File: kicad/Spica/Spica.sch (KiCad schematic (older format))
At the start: 8 parts

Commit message: Add some Akizuki parts
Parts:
- removed R?: R_Variable, symbol Device:R_Variable
- added RV1: 10k, symbol Device:R_POT
- added SW1: SW_SPDT, symbol Switch:SW_SPDT
- IC1: renamed from IC?; symbol SamacSys_Parts:TA48033S -> Spica-rescue:TA48033S-SamacSys_Parts
- U1: renamed from U?; symbol ESP32-DEVKITC-32D:ESP32-DEVKITC-32D -> Spica-rescue:ESP32-DEVKITC-32D-ESP32-DEVKITC-32D
- gave numbers to parts that had none: 5
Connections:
- wire segments 9 -> 18
- no-connect marks 0 -> 28
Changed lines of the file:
@@
 EESchema Schematic File Version 4
+LIBS:Spica-cache
 EELAYER 26 0
 EELAYER END
@@
 $EndDescr
 $Comp
-L ESP32-DEVKITC-32D:ESP32-DEVKITC-32D U?
+L Spica-rescue:ESP32-DEVKITC-32D-ESP32-DEVKITC-32D U1
 U 1 1 5BDC6C5C
 P 8600 3300
-F 0 "U?" H 8600 4467 50  0000 C CNN
+F 0 "U1" H 8600 4467 50  0000 C CNN
 F 1 "ESP32-DEVKITC-32D" H 8600 4376 50  0000 C CNN
 F 2 "MODULE_ESP32-DEVKITC-32D" H 8600 3300 50  0001 L BNN
@@
 $EndComp
 $Comp
-L Motor:Motor_DC M?
+L Motor:Motor_DC M2
 U 1 1 5BDC7764
 P 3000 1650
-F 0 "M?" H 3158 1646 50  0000 L CNN
+F 0 "M2" H 3158 1646 50  0000 L CNN
 F 1 "Motor_DC" H 3158 1555 50  0000 L CNN
 F 2 "Connector_JST:JST_XH_B02B-XH-A_1x02_P2.50mm_Vertical" H 3000 1560 50  0001 C CNN
@@
 $EndComp
 $Comp
-L Motor:Motor_DC M?
+L Motor:Motor_DC M1
 U 1 1 5BDC782D
 P 2250 1650
-F 0 "M?" H 2408 1646 50  0000 L CNN
+F 0 "M1" H 2408 1646 50  0000 L CNN
 F 1 "Motor_DC" H 2408 1555 50  0000 L CNN
 F 2 "Connector_JST:JST_XH_B02B-XH-A_1x02_P2.50mm_Vertical" H 2250 1560 50  0001 C CNN
@@
 $EndComp
 $Comp
-L SamacSys_Parts:TA48033S IC?
+L Spica-rescue:TA48033S-SamacSys_Parts IC1
 U 1 1 5BDC796A
 P 2700 4100
-F 0 "IC?" H 3200 4365 50  0000 C CNN
+F 0 "IC1" H 3200 4365 50  0000 C CNN
 F 1 "TA48033S" H 3200 4274 50  0000 C CNN
 F 2 "TO254P490X1000X2090-3P" H 3550 4200 50  0001 L CNN
@@
 L power:VCC #PWR0101
 U 1 1 5BDC7FCD
-P 1150 4100
-F 0 "#PWR0101" H 1150 3950 50  0001 C CNN
-F 1 "VCC" H 1167 4273 50  0000 C CNN
-F 2 "" H 1150 4100 50  0001 C CNN
-F 3 "" H 1150 4100 50  0001 C CNN
-	1    1150 4100
+P 750 4100
+F 0 "#PWR0101" H 750 3950 50  0001 C CNN
+F 1 "VCC" H 767 4273 50  0000 C CNN
+F 2 "" H 750 4100 50  0001 C CNN
+F 3 "" H 750 4100 50  0001 C CNN
+	1    750  4100
 	1    0    0    -1
 $EndComp
@@
 $EndComp
 $Comp
-L Device:C C?
+L Device:C C2
 U 1 1 5BDC8EDA
 P 2200 4250
-F 0 "C?" H 2315 4296 50  0000 L CNN
+F 0 "C2" H 2315 4296 50  0000 L CNN
 F 1 "C" H 2315 4205 50  0000 L CNN
 F 2 "" H 2238 4100 50  0001 C CNN
@@
 $EndComp
 $Comp
-L Device:CP C?
+L Device:CP C3
 U 1 1 5BDC96DE
 P 3900 4250
-F 0 "C?" H 4018 4296 50  0000 L CNN
+F 0 "C3" H 4018 4296 50  0000 L CNN
 F 1 "CP" H 4018 4205 50  0000 L CNN
 F 2 "" H 3938 4100 50  0001 C CNN
@@
 $EndComp
 $Comp
-L Device:CP C?
+L Device:CP C1
 U 1 1 5BDCB405
 P 1850 4250
-F 0 "C?" H 1968 4296 50  0000 L CNN
+F 0 "C1" H 1968 4296 50  0000 L CNN
 F 1 "CP" H 1968 4205 50  0000 L CNN
 F 2 "" H 1888 4100 50  0001 C CNN
@@
 $EndComp
 Wire Wire Line
-	1150 4100 1850 4100
-Wire Wire Line
 	2200 4100 1850 4100
 Connection ~ 2200 4100
+$Comp
+L power:GND #PWR0115
+U 1 1 5BDD17C0
+P 6450 3250
+F 0 "#PWR0115" H 6450 3000 50  0001 C CNN
+F 1 "GND" H 6455 3077 50  0000 C CNN
+F 2 "" H 6450 3250 50  0001 C CNN
+F 3 "" H 6450 3250 50  0001 C CNN
+	1    6450 3250
+	1    0    0    -1
+$EndComp
+$Comp
+L power:+3.3V #PWR0116
+U 1 1 5BDD1968
+P 6450 2950
+F 0 "#PWR0116" H 6450 2800 50  0001 C CNN
+F 1 "+3.3V" H 6465 3123 50  0000 C CNN
+F 2 "" H 6450 2950 50  0001 C CNN
+F 3 "" H 6450 2950 50  0001 C CNN
+	1    6450 2950
+	1    0    0    -1
+$EndComp
+$Comp
+L Switch:SW_SPDT SW1
+U 1 1 5BDD2829
+P 1150 4100
+F 0 "SW1" H 1150 4385 50  0000 C CNN
+F 1 "SW_SPDT" H 1150 4294 50  0000 C CNN
+F 2 "" H 1150 4100 50  0001 C CNN
+F 3 "" H 1150 4100 50  0001 C CNN
+	1    1150 4100
+	1    0    0    -1
+$EndComp
+Wire Wire Line
+	1350 4000 1850 4000
+Wire Wire Line
+	1850 4000 1850 4100
 Connection ~ 1850 4100
-$Comp
-L Device:R_Variable R?
-U 1 1 5BDCC0C1
-P 6950 3350
-F 0 "R?" H 7078 3396 50  0000 L CNN
-F 1 "R_Variable" H 7078 3305 50  0000 L CNN
-F 2 "" V 6880 3350 50  0001 C CNN
-F 3 "~" H 6950 3350 50  0001 C CNN
-	1    6950 3350
-	1    0    0    -1
-$EndComp
+Wire Wire Line
+	950  4100 750  4100
+NoConn ~ 1350 4200
+NoConn ~ 7800 2500
+NoConn ~ 7800 2600
+NoConn ~ 7800 2700
+$Comp
+L Device:R_POT RV1
+U 1 1 5BDD441D
+P 6450 3100
+F 0 "RV1" H 6380 3146 50  0000 R CNN
+F 1 "10k" H 6380 3055 50  0000 R CNN
+F 2 "" H 6450 3100 50  0001 C CNN
+F 3 "~" H 6450 3100 50  0001 C CNN
+	1    6450 3100
+	1    0    0    -1
+$EndComp
+Wire Wire Line
+	6600 3100 7800 3100
+NoConn ~ 7800 2800
+NoConn ~ 7800 2900
+NoConn ~ 7800 3000
+NoConn ~ 7800 3400
+NoConn ~ 7800 3500
+NoConn ~ 7800 3600
+NoConn ~ 7800 3800
+NoConn ~ 7800 3900
+NoConn ~ 7800 4000
+NoConn ~ 7800 4100
+NoConn ~ 7800 4200
+Wire Wire Line
+	9400 2500 10100 2500
+Wire Wire Line
+	9400 2600 10100 2600
+NoConn ~ 9400 2700
+NoConn ~ 9400 2800
+NoConn ~ 9400 2900
+Wire Wire Line
+	9400 3400 10100 3400
+Wire Wire Line
+	9400 3500 10100 3500
+NoConn ~ 9400 3100
+NoConn ~ 9400 3200
+NoConn ~ 9400 3300
+NoConn ~ 9400 3600
+NoConn ~ 9400 3700
+NoConn ~ 9400 3800
+NoConn ~ 9400 3900
+NoConn ~ 9400 4000
+NoConn ~ 9400 4100
+NoConn ~ 9400 4200
+Wire Wire Line
+	7800 3200 7250 3200
+Wire Wire Line
+	7800 3300 7250 3300
 $EndSCHEMATC

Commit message: Finish rooting
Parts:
- added BT1: Battery_Cell, Connector_JST:JST_XH_B02B-XH-A_1x02_P2.50mm_Vertical, symbol Device:Battery_Cell
- added U2: DRV8835-akizuki, Package_DIP:DIP-12_W7.62mm_LongPads, symbol drv8835-akizuki:DRV8835-akizuki
- added U3: HC-SR04, HC-SR04:XCVR_HC-SR04, symbol HC-SR04:HC-SR04
- added U4: AE-XCL102D503CR-G, Package_DIP:DIP-6_W7.62mm_Socket, symbol xcl102-akizuki:AE-XCL102D503CR-G
- C1: value CP -> 1000μ; footprint (none) -> Capacitor_THT:CP_Radial_D10.0mm_P5.00mm
- C2: value C -> 0.1μ; footprint (none) -> Capacitor_THT:C_Disc_D3.0mm_W2.0mm_P2.50mm
- C3: value CP -> 100μ; footprint (none) -> Capacitor_THT:CP_Radial_D5.0mm_P2.50mm
- IC1: symbol Spica-rescue:TA48033S-SamacSys_Parts -> TA48033S:TA48033S
- RV1: footprint (none) -> TSR-065-103-R:TSR065103R
- SW1: footprint (none) -> Connector_PinSocket_2.54mm:PinSocket_1x03_P2.54mm_Vertical
- U1: symbol Spica-rescue:ESP32-DEVKITC-32D-ESP32-DEVKITC-32D -> ESP32-DEVKITC-32D:ESP32-DEVKITC-32D
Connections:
- net labels added: 3.3V, 5V, IO16, IO17, IO22, IO23, IO25, IO26
- net labels removed: +3.3V
- wire segments 18 -> 33
- no-connect marks 28 -> 29
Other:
- moved on the sheet: C1, C2, C3, IC1, M1, M2, SW1

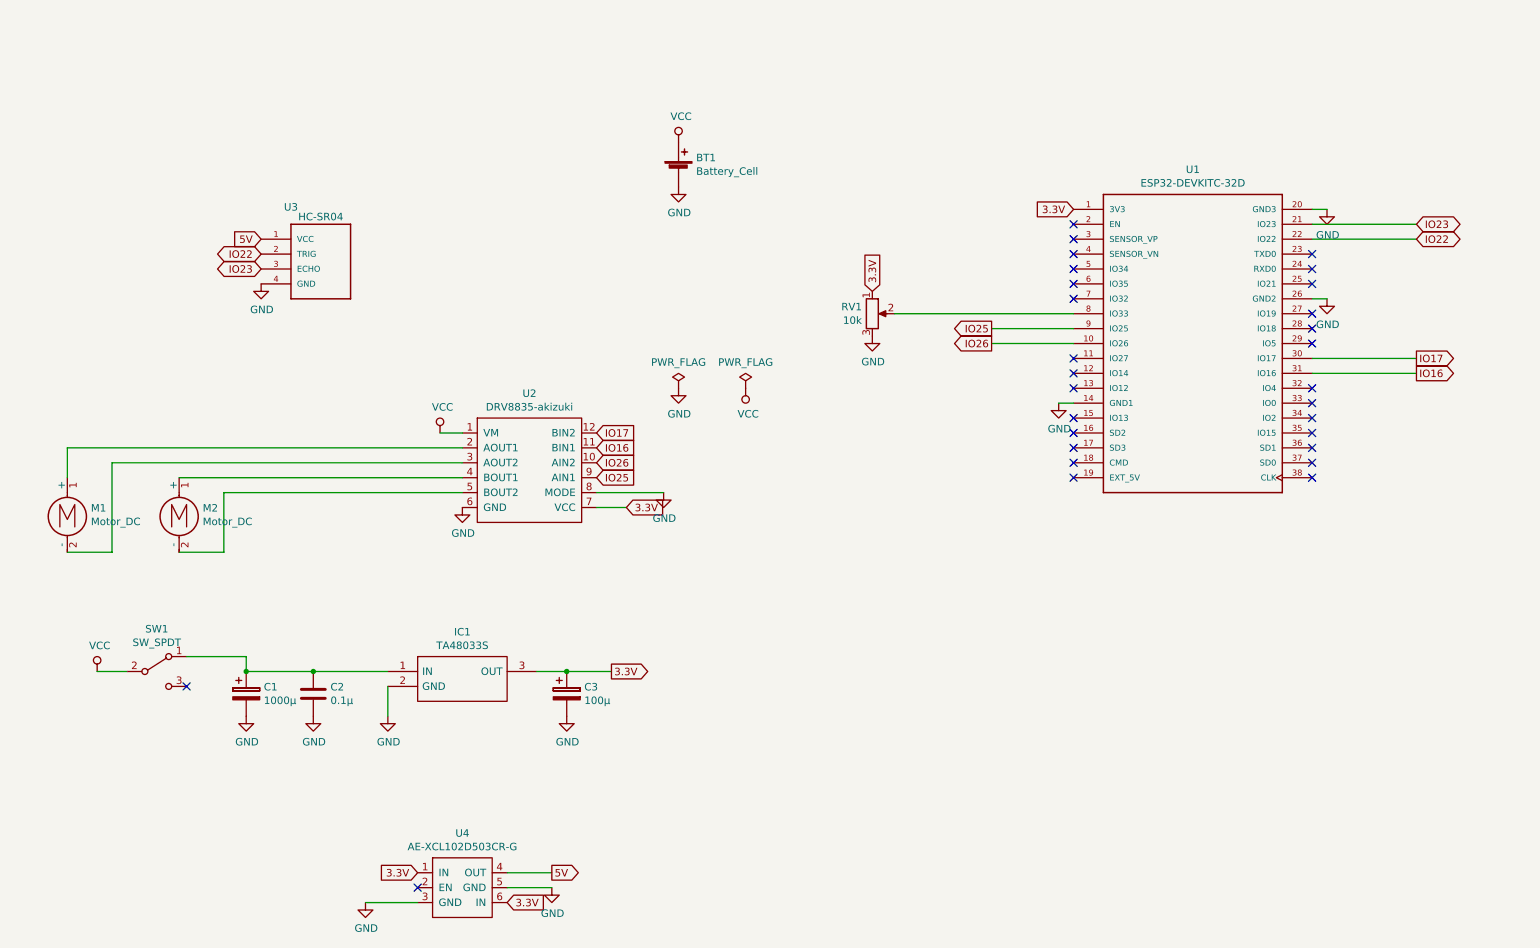
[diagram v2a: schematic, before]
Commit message: Add surface GND
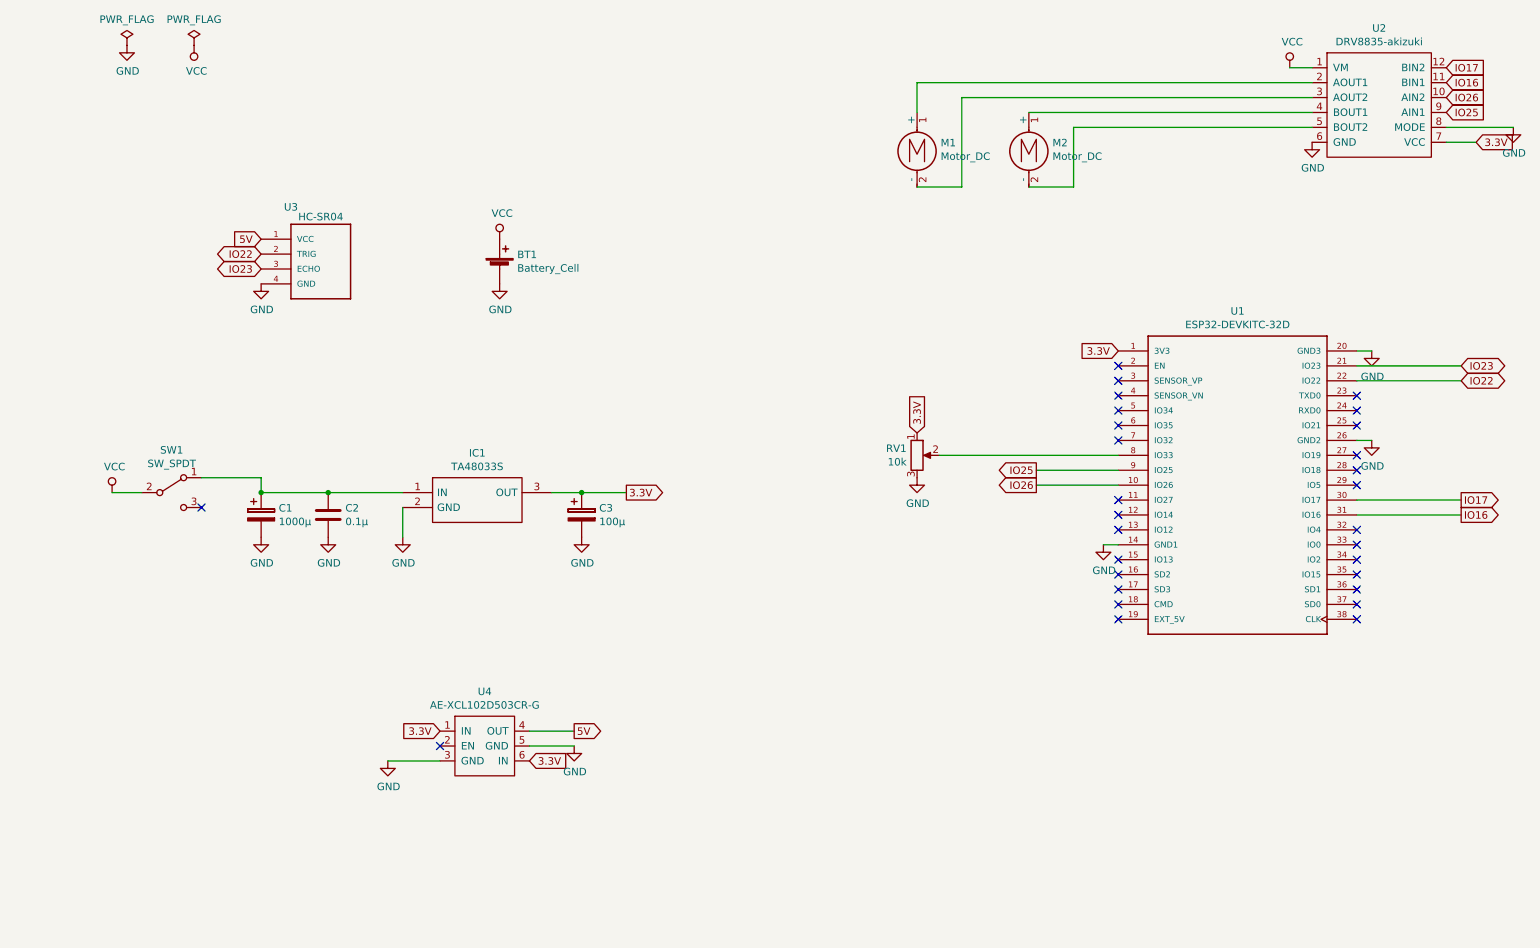
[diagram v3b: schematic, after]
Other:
- moved on the sheet: BT1, C1, C2, C3, IC1, M1, M2, RV1, SW1, U1, U2, U4

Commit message: ベタパターンを追加
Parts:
- added C4: 0.1μ, Capacitor_THT:C_Disc_D3.0mm_W2.0mm_P2.50mm, symbol Device:C
- added C5: 10μ, Capacitor_THT:CP_Radial_D5.0mm_P2.50mm, symbol Device:CP
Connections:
- net 3.3V: now also C4.1
- net 5V: now also C5.1
- net GND: now also C4.2, C5.2
- net VCC: now also C1.1, C2.1, IC1.1 (IN); no longer BT1.1 (+)
- new net: BT1.1 (+), SW1.1 (A)
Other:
- moved on the sheet: SW1
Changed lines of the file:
@@
 L power:VCC #PWR0101
 U 1 1 5BDC7FCD
-P 1350 4300
-F 0 "#PWR0101" H 1350 4150 50  0001 C CNN
-F 1 "VCC" H 1367 4473 50  0000 C CNN
-F 2 "" H 1350 4300 50  0001 C CNN
-F 3 "" H 1350 4300 50  0001 C CNN
-	1    1350 4300
+P 2350 4200
+F 0 "#PWR0101" H 2350 4050 50  0001 C CNN
+F 1 "VCC" H 2367 4373 50  0000 C CNN
+F 2 "" H 2350 4200 50  0001 C CNN
+F 3 "" H 2350 4200 50  0001 C CNN
+	1    2350 4200
 	1    0    0    -1
 $EndComp
@@
 	4300 4300 4500 4300
 Wire Wire Line
-	4800 4300 4500 4300
-Connection ~ 4500 4300
-Wire Wire Line
 	3300 4400 3300 4600
 Wire Wire Line
@@
 L Switch:SW_SPDT SW1
 U 1 1 5BDD2829
-P 1750 4300
-F 0 "SW1" H 1750 4585 50  0000 C CNN
-F 1 "SW_SPDT" H 1750 4494 50  0000 C CNN
-F 2 "Connector_PinSocket_2.54mm:PinSocket_1x03_P2.54mm_Vertical" H 1750 4300 50  0001 C CNN
-F 3 "" H 1750 4300 50  0001 C CNN
-	1    1750 4300
-	1    0    0    -1
-$EndComp
-Wire Wire Line
-	1950 4200 2350 4200
+P 3850 2000
+F 0 "SW1" H 3850 2285 50  0000 C CNN
+F 1 "SW_SPDT" H 3850 2194 50  0000 C CNN
+F 2 "Connector_PinSocket_2.54mm:PinSocket_1x03_P2.54mm_Vertical" H 3850 2000 50  0001 C CNN
+F 3 "" H 3850 2000 50  0001 C CNN
+	1    3850 2000
+	0    1    1    0
+$EndComp
+Wire Wire Line
+	3950 2200 3950 2600
 Wire Wire Line
 	2350 4200 2350 4300
 Wire Wire Line
-	1550 4300 1350 4300
-NoConn ~ 1950 4400
+	3850 1800 3850 1600
+NoConn ~ 3750 2200
 NoConn ~ 8100 3450
 NoConn ~ 8100 3550
@@
 $EndComp
 Wire Wire Line
-	4150 5900 4450 5900
+	4700 5900 5000 5900
 Wire Wire Line
 	4150 6000 4450 6000
@@
 	1    0    0    1
 $EndComp
-Text GLabel 4800 4300 2    50   Output ~ 0
+Text GLabel 5350 4300 2    50   Output ~ 0
 3.3V
 Text GLabel 4150 6100 2    50   Input ~ 0
@@
 Text GLabel 8100 3350 0    50   Input ~ 0
 3.3V
-Text GLabel 4450 5900 2    50   Output ~ 0
+Text GLabel 5000 5900 2    50   Output ~ 0
 5V
 Text GLabel 2350 2600 0    50   Input ~ 0
@@
 L power:VCC #PWR0107
 U 1 1 5BE37EE1
-P 3950 2600
-F 0 "#PWR0107" H 3950 2450 50  0001 C CNN
-F 1 "VCC" H 3967 2773 50  0000 C CNN
-F 2 "" H 3950 2600 50  0001 C CNN
-F 3 "" H 3950 2600 50  0001 C CNN
-	1    3950 2600
+P 3850 1600
+F 0 "#PWR0107" H 3850 1450 50  0001 C CNN
+F 1 "VCC" H 3867 1773 50  0000 C CNN
+F 2 "" H 3850 1600 50  0001 C CNN
+F 3 "" H 3850 1600 50  0001 C CNN
+	1    3850 1600
 	1    0    0    -1
 $EndComp
@@
 	1    0    0    -1
 $EndComp
+$Comp
+L power:GND #PWR0116
+U 1 1 5BE29AAF
+P 4700 6200
+F 0 "#PWR0116" H 4700 5950 50  0001 C CNN
+F 1 "GND" H 4705 6027 50  0000 C CNN
+F 2 "" H 4700 6200 50  0001 C CNN
+F 3 "" H 4700 6200 50  0001 C CNN
+	1    4700 6200
+	1    0    0    -1
+$EndComp
+$Comp
+L Device:CP C5
+U 1 1 5BE29AB5
+P 4700 6050
+F 0 "C5" H 4818 6096 50  0000 L CNN
+F 1 "10μ" H 4818 6005 50  0000 L CNN
+F 2 "Capacitor_THT:CP_Radial_D5.0mm_P2.50mm" H 4738 5900 50  0001 C CNN
+F 3 "~" H 4700 6050 50  0001 C CNN
+	1    4700 6050
+	1    0    0    -1
+$EndComp
+Connection ~ 4500 4300
+Wire Wire Line
+	4150 5900 4700 5900
+Connection ~ 4700 5900
+Wire Wire Line
+	4500 4300 5000 4300
+$Comp
+L power:GND #PWR0112
+U 1 1 5BE2D939
+P 5000 4600
+F 0 "#PWR0112" H 5000 4350 50  0001 C CNN
+F 1 "GND" H 5005 4427 50  0000 C CNN
+F 2 "" H 5000 4600 50  0001 C CNN
+F 3 "" H 5000 4600 50  0001 C CNN
+	1    5000 4600
+	1    0    0    -1
+$EndComp
+$Comp
+L Device:C C4
+U 1 1 5BE2D93F
+P 5000 4450
+F 0 "C4" H 5115 4496 50  0000 L CNN
+F 1 "0.1μ" H 5115 4405 50  0000 L CNN
+F 2 "Capacitor_THT:C_Disc_D3.0mm_W2.0mm_P2.50mm" H 5038 4300 50  0001 C CNN
+F 3 "~" H 5000 4450 50  0001 C CNN
+	1    5000 4450
+	1    0    0    -1
+$EndComp
+Connection ~ 5000 4300
+Wire Wire Line
+	5000 4300 5350 4300
 $EndSCHEMATC
